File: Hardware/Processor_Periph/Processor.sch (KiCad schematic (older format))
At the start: 187 parts, among them J1 UART0, J10 JTAGICE3-SWD, J2 5V, J3 USB_OTG, J4 RJ-45_J0006D01BNL, J5 Micro_SD_Card, J6 I2C, J7 PWM, J8 Spare0, J9 Spare1, Q1 BSS806NE, Q2 BSS806NE, Q3 BSS806NE, Q4 BSS806NE, SW1 ~RST, SW2 PB, SW3 PB, U1 TXS0102, U10 Oscillator, U11 CY7C1018, U2 LM3671, U3 S25FL127S, U4 PRTR5V0U2X, U5 MIC5365, U6 DSC61XX, U7 DP83848C, U8 ATSAM4E16E, U9 3.0V, Y1 32.768kHz

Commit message: Fixed ERC issues, added reverse polarity protection diode
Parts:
- removed R32, R33: 0R, symbol R
- added D6: PMEG6030ETP, FritzLib:SOD-128, symbol D_Schottky_Small_ALT
- added R27, R34, R35: 0R, symbol R
- renumbered R34 to R24, R24 to R25, R25 to R26, R26 to R28, R27 to R29, R28 to R30, R29 to R31, R30 to R32, R31 to R33, R35 to R36, R36 to R37, R37 to R38, R38 to R39, R39 to R40, R40 to R41, R41 to R42, R42 to R43, R43 to R44, R44 to R45, R45 to R46, R46 to R47, R47 to R48, R48 to R49, R49 to R50, R50 to R51, R51 to R52, R52 to R53, R53 to R54, R54 to R55, R55 to R56, R56 to R57, R57 to R58, R58 to R59, R59 to R60, R60 to R61, R61 to R62, R62 to R63, R63 to R64, R64 to R65, R65 to R66, R66 to R67, R67 to R68, R68 to R69, R69 to R70, R70 to R71, R71 to R72, R72 to R73, R73 to R74, R74 to R75, R75 to R76, R76 to R77, R77 to R78, R78 to R79, R79 to R80
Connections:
- net labels removed: PB1
- wire segments 796 -> 1014
- no-connect marks 15 -> 16
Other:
- note added: "Replace 0R w/Ferrite \nBeads if EMI is an issue"
- moved on the sheet: J2, R24, R49, R50, R51, R52, R54, R55, R56, R57, R60, R61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

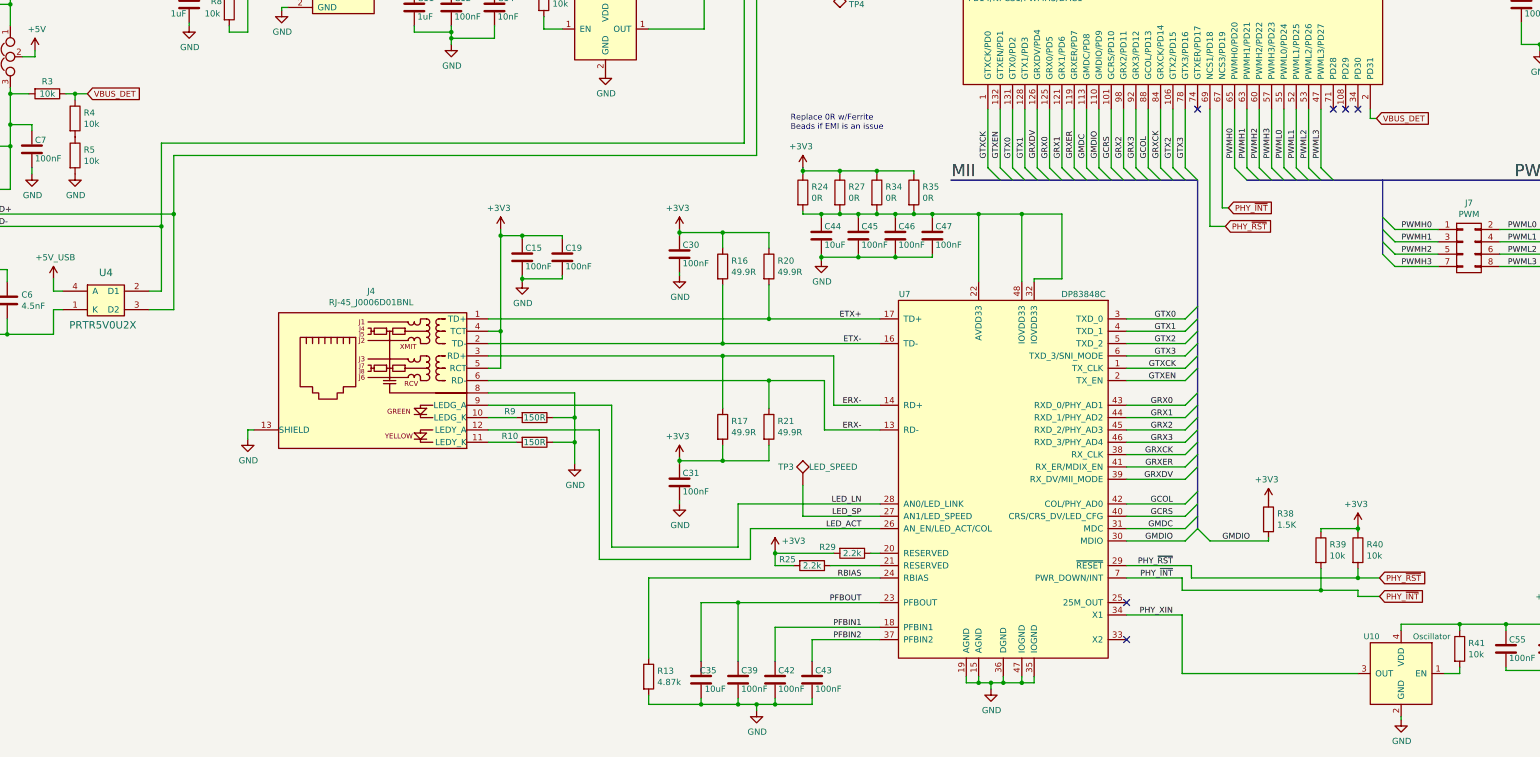
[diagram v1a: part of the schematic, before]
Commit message: Cleaned up schematic
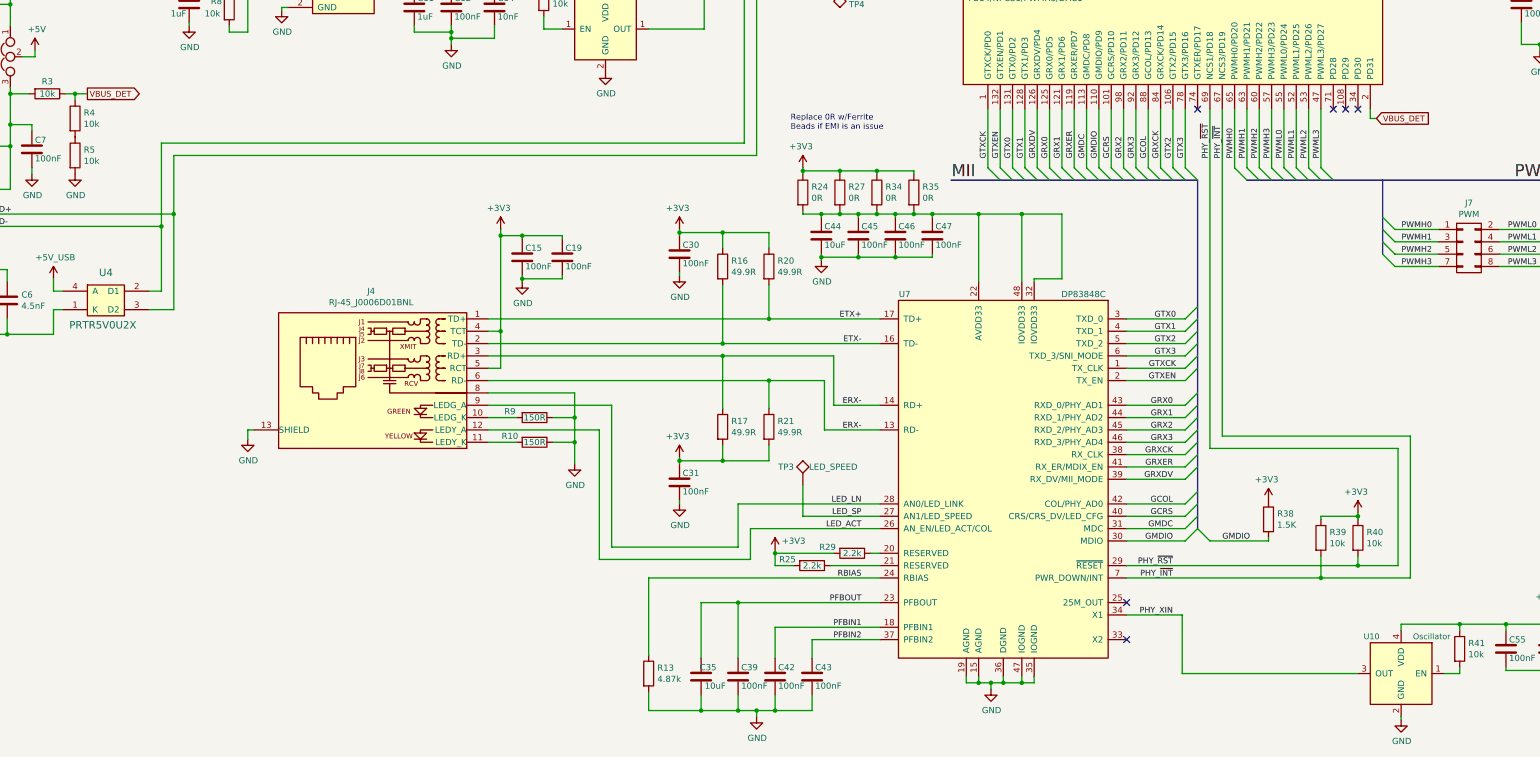
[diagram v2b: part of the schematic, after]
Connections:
- wire segments 1014 -> 1010
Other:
- moved on the sheet: C35, C39, C42, C43, R13, R39, R40
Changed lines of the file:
@@
 Text GLabel 14025 10150 2    47   Input ~ 0
 VBUS_DET
-Text GLabel 3575 9950 2    47   Input ~ 0
+Text GLabel 3575 9950 2    47   Output ~ 0
 VBUS_DET
 $Comp
@@
 L C C35
 U 1 1 58C1B446
-P 8550 14700
-F 0 "C35" H 8425 14775 50  0000 L CNN
-F 1 "10uF" H 8350 14625 50  0000 L CNN
-F 2 "Capacitors_SMD:C_0805" H -1737 9625 50  0001 C CNN
-F 3 "" H -1775 9775 50  0001 C CNN
-	1    8550 14700
+P 8550 14675
+F 0 "C35" H 8425 14750 50  0000 L CNN
+F 1 "10uF" H 8350 14600 50  0000 L CNN
+F 2 "Capacitors_SMD:C_0805" H -1737 9600 50  0001 C CNN
+F 3 "" H -1775 9750 50  0001 C CNN
+	1    8550 14675
 	-1   0    0    -1
 $EndComp
@@
 L C C39
 U 1 1 58C22208
-P 8850 14700
-F 0 "C39" H 8875 14775 50  0000 L CNN
-F 1 "100nF" H 8875 14625 50  0000 L CNN
-F 2 "Capacitors_SMD:C_0603" H -1437 9625 50  0001 C CNN
-F 3 "" H -1475 9775 50  0001 C CNN
-	1    8850 14700
+P 8850 14675
+F 0 "C39" H 8875 14750 50  0000 L CNN
+F 1 "100nF" H 8875 14600 50  0000 L CNN
+F 2 "Capacitors_SMD:C_0603" H -1437 9600 50  0001 C CNN
+F 3 "" H -1475 9750 50  0001 C CNN
+	1    8850 14675
 	1    0    0    -1
 $EndComp
@@
 L C C42
 U 1 1 58C243AA
-P 9150 14700
-F 0 "C42" H 9175 14775 50  0000 L CNN
-F 1 "100nF" H 9175 14625 50  0000 L CNN
-F 2 "Capacitors_SMD:C_0603" H -1137 9625 50  0001 C CNN
-F 3 "" H -1175 9775 50  0001 C CNN
-	1    9150 14700
+P 9150 14675
+F 0 "C42" H 9175 14750 50  0000 L CNN
+F 1 "100nF" H 9175 14600 50  0000 L CNN
+F 2 "Capacitors_SMD:C_0603" H -1137 9600 50  0001 C CNN
+F 3 "" H -1175 9750 50  0001 C CNN
+	1    9150 14675
 	1    0    0    -1
 $EndComp
@@
 L C C43
 U 1 1 58C24AF8
-P 9450 14700
-F 0 "C43" H 9475 14775 50  0000 L CNN
-F 1 "100nF" H 9475 14625 50  0000 L CNN
-F 2 "Capacitors_SMD:C_0603" H -837 9625 50  0001 C CNN
-F 3 "" H -875 9775 50  0001 C CNN
-	1    9450 14700
+P 9450 14675
+F 0 "C43" H 9475 14750 50  0000 L CNN
+F 1 "100nF" H 9475 14600 50  0000 L CNN
+F 2 "Capacitors_SMD:C_0603" H -837 9600 50  0001 C CNN
+F 3 "" H -875 9750 50  0001 C CNN
+	1    9450 14675
 	1    0    0    -1
 $EndComp
@@
 L GND #PWR064
 U 1 1 58C251B2
-P 9000 14950
-F 0 "#PWR064" H 6950 7900 50  0001 C CNN
-F 1 "GND" H 9005 14777 50  0000 C CNN
-F 2 "" H 6950 8150 50  0001 C CNN
-F 3 "" H 6950 8150 50  0001 C CNN
-	1    9000 14950
+P 9000 15000
+F 0 "#PWR064" H 6950 7950 50  0001 C CNN
+F 1 "GND" H 9005 14827 50  0000 C CNN
+F 2 "" H 6950 8200 50  0001 C CNN
+F 3 "" H 6950 8200 50  0001 C CNN
+	1    9000 15000
 	1    0    0    -1
 $EndComp
@@
 L R R40
 U 1 1 58FCC7EB
-P 13875 13650
-F 0 "R40" H 13945 13696 50  0000 L CNN
-F 1 "10k" H 13945 13605 50  0000 L CNN
-F 2 "Capacitors_SMD:C_0603" V 11805 5675 50  0001 C CNN
-F 3 "" H 11875 5675 50  0001 C CNN
-	1    13875 13650
+P 13875 13550
+F 0 "R40" H 13945 13596 50  0000 L CNN
+F 1 "10k" H 13945 13505 50  0000 L CNN
+F 2 "Capacitors_SMD:C_0603" V 11805 5575 50  0001 C CNN
+F 3 "" H 11875 5575 50  0001 C CNN
+	1    13875 13550
 	1    0    0    -1
 $EndComp
@@
 L +3V3 #PWR085
 U 1 1 58FCE5C3
-P 13875 13450
-F 0 "#PWR085" H 13925 13500 50  0001 C CNN
-F 1 "+3V3" H 13890 13623 50  0000 C CNN
-F 2 "" H 4150 9225 50  0001 C CNN
-F 3 "" H 4150 9225 50  0001 C CNN
-	1    13875 13450
+P 13875 13350
+F 0 "#PWR085" H 13925 13400 50  0001 C CNN
+F 1 "+3V3" H 13890 13523 50  0000 C CNN
+F 2 "" H 4150 9125 50  0001 C CNN
+F 3 "" H 4150 9125 50  0001 C CNN
+	1    13875 13350
 	-1   0    0    -1
 $EndComp
 Text Label 12375 13775 2    47   ~ 0
 PHY_~RST
-Text GLabel 14050 13875 2    47   Input ~ 0
-PHY_~RST
-Text GLabel 12800 11025 2    47   Input ~ 0
-PHY_~RST
 $Comp
 L R R22
@@
 Text Label 10075 4775 0    47   ~ 0
 I2C_SDA
-Text GLabel 14050 14025 2    47   Input ~ 0
-PHY_~INT
 Entry Wire Line
 	12675 13575 12575 13475
@@
 L R R39
 U 1 1 59087037
-P 13575 13650
-F 0 "R39" H 13645 13696 50  0000 L CNN
-F 1 "10k" H 13645 13605 50  0000 L CNN
-F 2 "Capacitors_SMD:C_0603" V 11505 5675 50  0001 C CNN
-F 3 "" H 11575 5675 50  0001 C CNN
-	1    13575 13650
+P 13575 13550
+F 0 "R39" H 13645 13596 50  0000 L CNN
+F 1 "10k" H 13645 13505 50  0000 L CNN
+F 2 "Capacitors_SMD:C_0603" V 11505 5575 50  0001 C CNN
+F 3 "" H 11575 5575 50  0001 C CNN
+	1    13575 13550
 	1    0    0    -1
 $EndComp
@@
 L R R13
 U 1 1 5908C698
-P 8125 14675
-F 0 "R13" H 8195 14721 50  0000 L CNN
-F 1 "4.87k" H 8195 14630 50  0000 L CNN
-F 2 "" V 8055 14675 50  0001 C CNN
-F 3 "" H 8125 14675 50  0001 C CNN
-	1    8125 14675
+P 8125 14650
+F 0 "R13" H 8195 14696 50  0000 L CNN
+F 1 "4.87k" H 8195 14605 50  0000 L CNN
+F 2 "" V 8055 14650 50  0001 C CNN
+F 3 "" H 8125 14650 50  0001 C CNN
+	1    8125 14650
 	1    0    0    -1
 $EndComp
@@
 Text Label 21900 13925 2    47   ~ 0
 GRXER
-Text GLabel 12825 10875 2    47   Input ~ 0
-PHY_~INT
 NoConn ~ 12575 10075
 NoConn ~ 10475 8575
@@
 	13675 10650 15475 10650
 Wire Wire Line
-	12775 10875 12825 10875
-Wire Wire Line
-	12775 10075 12775 10875
+	12775 10075 12775 12725
 Wire Notes Line
 	22100 12675 22100 12925
@@
 	8125 13875 10000 13875
 Wire Wire Line
-	8125 14525 8125 13875
-Connection ~ 8550 14900
+	8125 14500 8125 13875
+Connection ~ 8550 14950
 Wire Wire Line
-	8125 14825 8125 14900
-Connection ~ 13875 13475
+	8125 14800 8125 14950
+Connection ~ 13875 13375
 Wire Wire Line
-	13575 13475 13575 13500
+	13575 13375 13575 13400
 Wire Wire Line
-	13875 13475 13575 13475
-Connection ~ 13575 13975
+	13875 13375 13575 13375
+Connection ~ 13575 13875
 Wire Wire Line
-	13575 13800 13575 13975
+	13575 13700 13575 13875
 Wire Wire Line
 	9375 13375 10000 13375
@@
 	13150 13575 13150 13550
 Wire Wire Line
-	12450 13975 13575 13975
-Wire Wire Line
-	13575 13975 13875 13975
-Wire Wire Line
-	12450 13875 12450 13975
-Wire Wire Line
-	12000 13875 12450 13875
-Wire Wire Line
-	12525 13875 13875 13875
+	12000 13875 13575 13875
 Wire Wire Line
-	13875 13875 14050 13875
+	13575 13875 14300 13875
 Wire Wire Line
-	12525 13775 12525 13875
+	12000 13775 13875 13775
 Wire Wire Line
-	12000 13775 12525 13775
+	13875 13775 14200 13775
 Wire Wire Line
 	12675 13575 13150 13575
-Wire Wire Line
-	13875 14025 14050 14025
-Wire Wire Line
-	13875 13975 13875 14025
 Connection ~ 9075 4575
 Connection ~ 9675 4675
@@
 	9025 4175 9025 4150
 Wire Wire Line
-	12675 11025 12800 11025
-Wire Wire Line
-	12675 10075 12675 11025
-Connection ~ 13875 13875
+	12675 10075 12675 12825
+Connection ~ 13875 13775
 Wire Wire Line
-	13875 13450 13875 13475
+	13875 13350 13875 13375
 Wire Wire Line
-	13875 13475 13875 13500
+	13875 13375 13875 13400
 Wire Wire Line
-	13875 13875 13875 13800
+	13875 13775 13875 13700
 Connection ~ 7525 12575
 Wire Wire Line
@@
 Connection ~ 8850 14075
 Wire Wire Line
-	8550 14550 8550 14075
+	8550 14525 8550 14075
 Wire Wire Line
 	8550 14075 8850 14075
@@
 	8850 14075 10000 14075
 Wire Wire Line
-	8850 14550 8850 14075
+	8850 14525 8850 14075
 Wire Wire Line
-	9150 14275 9150 14550
+	9150 14275 9150 14525
 Wire Wire Line
 	10000 14275 9150 14275
 Wire Wire Line
-	9450 14375 9450 14550
+	9450 14375 9450 14525
 Wire Wire Line
 	10000 14375 9450 14375
-Connection ~ 9000 14900
-Connection ~ 8850 14900
+Connection ~ 9000 14950
+Connection ~ 8850 14950
 Wire Wire Line
-	8850 14900 8850 14850
-Connection ~ 9150 14900
+	8850 14950 8850 14825
+Connection ~ 9150 14950
 Wire Wire Line
-	9450 14900 9450 14850
+	9450 14950 9450 14825
 Wire Wire Line
-	9150 14900 9150 14850
+	9150 14950 9150 14825
 Wire Wire Line
-	9000 14900 9000 14950
+	9000 14950 9000 15000
 Wire Wire Line
-	8125 14900 8550 14900
+	8125 14950 8550 14950
 Wire Wire Line
-	8550 14900 8850 14900
+	8550 14950 8850 14950
 Wire Wire Line
-	8850 14900 9000 14900
+	8850 14950 9000 14950
 Wire Wire Line
-	9000 14900 9150 14900
+	9000 14950 9150 14950
 Wire Wire Line
-	9150 14900 9450 14900
+	9150 14950 9450 14950
 Wire Wire Line
-	8550 14850 8550 14900
+	8550 14825 8550 14950
 Connection ~ 2175 6850
 Wire Wire Line
@@
 	11250 11450 11475 11450
 Wire Wire Line
-	11475 11450 11475 10925
+	11475 10925 11475 11450
 Connection ~ 10800 10925
 Connection ~ 11150 10925
@@
 $EndComp
 Wire Wire Line
-	11475 10925 11150 10925
+	9375 10925 9525 10925
 Wire Wire Line
-	11150 10925 10800 10925
+	9525 10925 9675 10925
 Wire Wire Line
-	10800 10925 10425 10925
+	9675 10925 9825 10925
 Wire Wire Line
-	10425 10925 10275 10925
+	9825 10925 9975 10925
 Wire Wire Line
-	10275 10925 10125 10925
+	9975 10925 10125 10925
 Wire Wire Line
-	10125 10925 9975 10925
+	10125 10925 10275 10925
 Wire Wire Line
-	9975 10925 9825 10925
+	10275 10925 10425 10925
 Wire Wire Line
-	9825 10925 9675 10925
+	10425 10925 10800 10925
 Wire Wire Line
-	9675 10925 9525 10925
+	10800 10925 11150 10925
 Wire Wire Line
-	9525 10925 9375 10925
+	11150 10925 11475 10925
 $Comp
 L R R27
@@
 Text Label 9575 6175 2    98   ~ 0
 EBI
+Text Label 12675 10475 1    47   ~ 0
+PHY_~RST
+Text Label 12775 10475 1    47   ~ 0
+PHY_~INT
+Wire Wire Line
+	14300 13875 14300 12725
+Wire Wire Line
+	14200 13775 14200 12825
+Wire Wire Line
+	14200 12825 12675 12825
+Wire Wire Line
+	14300 12725 12775 12725
 $EndSCHEMATC

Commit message: Added termination resistors to PHY & cleaned up schematic
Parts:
- added R? (x11): 33R, Capacitors_SMD:C_0603, symbol R
- U10: value Oscillator -> ASE-25.000MHZ-LC-T
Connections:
- net labels added: GCOL_R, GCRS_R, GMDC_R, GMDIO_R, GRX0_R, GRX1_R, GRX2_R, GRX3_R, GRXCK_R, GRXDV_R, GRXER_R
- wire segments 1010 -> 1021
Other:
- moved on the sheet: C10, C11, C12, C14, C15, C19, C2, C30, C31, C35, C39, C42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

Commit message: Updated BOM
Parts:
- removed J7: PWM, symbol CONN_02X04
- added J7: PWM, symbol CONN_02X06
- added R92: 0R, symbol R
- added TP11: XOUT_32, Measurement_Points:Measurement_Point_Round-SMD-Pad_Small, symbol TEST
- added TP12: XIN_32, Measurement_Points:Measurement_Point_Round-SMD-Pad_Small, symbol TEST
- added TP13: MCU_XIN, Measurement_Points:Measurement_Point_Round-SMD-Pad_Small, symbol TEST
- added TP14: PHY_XIN, Measurement_Points:Measurement_Point_Round-SMD-Pad_Small, symbol TEST
- R81, R82, R83, R84, R85, R86, R87, R88, R89, R90, R91: renamed from R?; value 33R -> 27R
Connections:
- wire segments 1021 -> 817

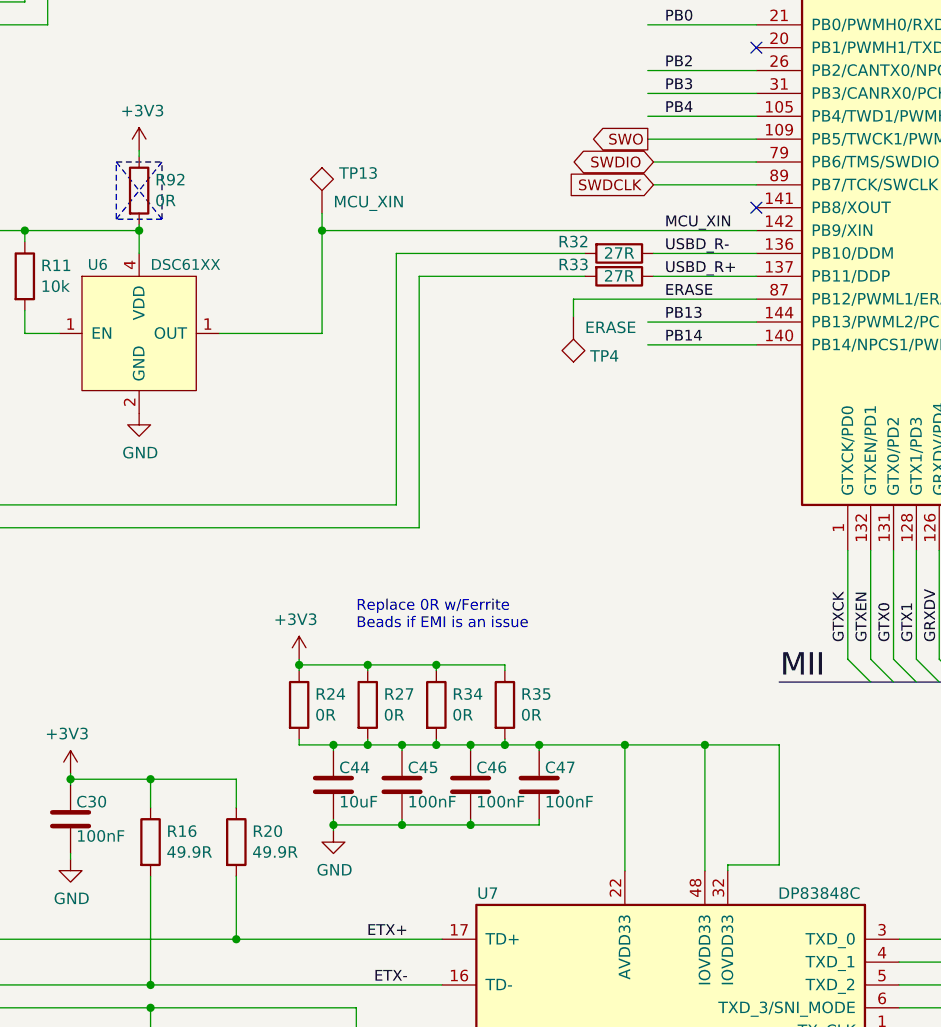
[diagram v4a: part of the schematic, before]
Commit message: Assigned some footprints, finished BOM
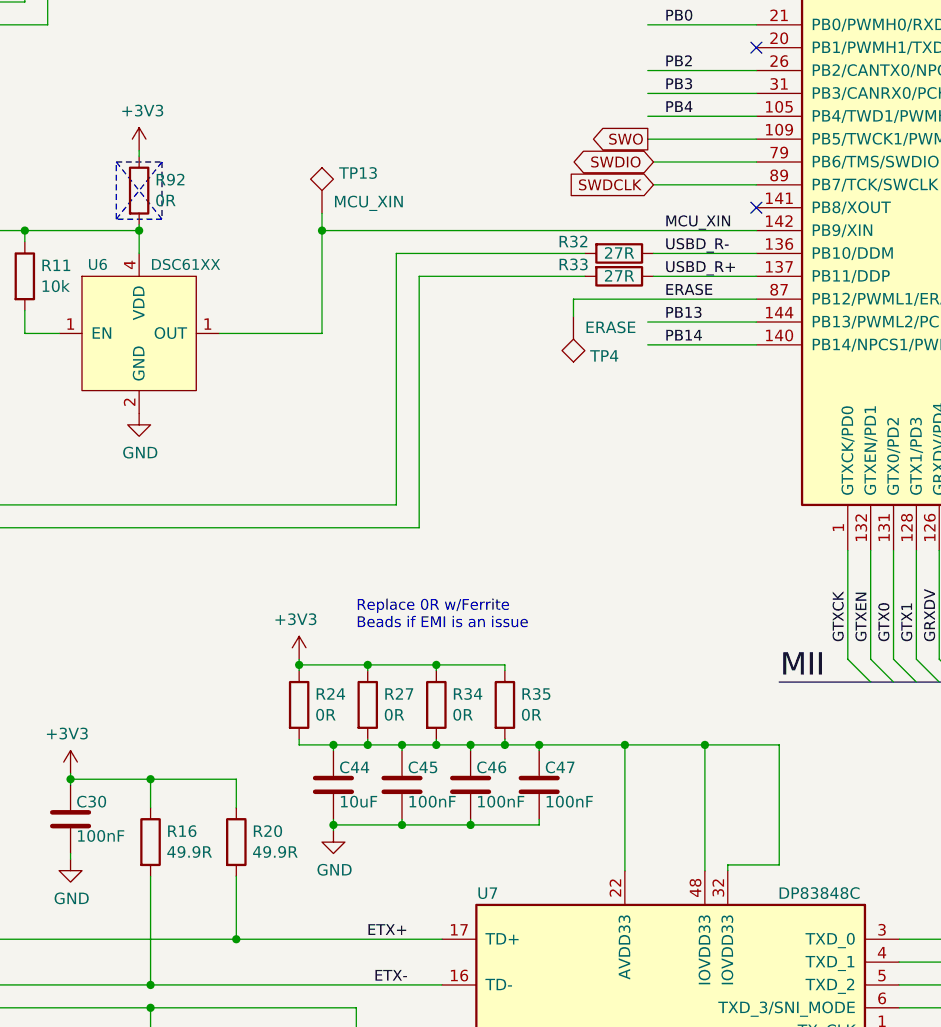
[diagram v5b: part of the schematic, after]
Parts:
- C10, C11, C44: footprint Capacitors_SMD:C_0603 -> Capacitors_SMD:C_0805
- D1, D2, D3, D4, D5: footprint LEDs:LED_0805 -> Diodes_SMD:D_0805
- J1: footprint FritzLib:ConnectorSMD-1x4 -> (none)
- J10: footprint FritzLib:ConnectorMicromatch-10 -> Pin_Headers:Pin_Header_Straight_2x05_Pitch1.27mm_SMD
- J2, JP1: footprint FritzLib:ConnectorSMD-1x3 -> (none)
- J3: footprint FritzLib:conn_usb_B_micro_smd -> (none)
- L1: footprint Inductors:Inductor_1212 -> (none)
- L2: footprint FritzLib:Inductor_3mmx3mm -> (none)
- Q1, Q2, Q3, Q4: footprint TO_SOT_Packages_SMD:SOT-23 -> (none)
- R1, R11, R12, R14, R15, R18, R19, R2, R22, R23, R25, R26, R28, R29, R3, R30, R31, R32, R33, R36, R37, R38, R39, R4, R40, R41, R42, R43, R44, R45, R46, R47, R48, R49, R5, R50, R51, R52, R54, R55, R56, R57, R58, R6, R60, R61, R62, R63, R64, R65, R66, R67, R68, R70, R71, R72, R73, R74, R75, R77, R78, R79, R8, R80, R81, R82, R83, R84, R85, R86, R87, R88, R89, R90, R91: footprint Capacitors_SMD:C_0603 -> Resistors_SMD:R_0603
- R10, R9: footprint Capacitors_SMD:C_0603 -> Resistors_SMD:R_0805
- R13, R16, R17, R20, R21, R24, R27, R34, R35, R92: footprint (none) -> Resistors_SMD:R_0603
- R53, R59, R69, R7, R76: footprint Capacitors_SMD:C_0805 -> Resistors_SMD:R_0805
- TP1, TP10, TP11, TP12, TP13, TP14, TP2, TP3, TP4, TP5, TP6, TP7, TP8, TP9: footprint Measurement_Points:Measurement_Point_Round-SMD-Pad_Small -> Measurement_Points:Test_Point_Keystone_5019_Minature
- U3: footprint (none) -> Housings_SOIC:SOIC-8_3.9x4.9mm_Pitch1.27mm
- U4: footprint FritzLib:SOT143B -> TO_SOT_Packages_SMD:SOT-143
- U5: footprint (none) -> TO_SOT_Packages_SMD:SOT-23-5
- U7: footprint LQFP-48 -> Housings_QFP:LQFP-48_7x7mm_Pitch0.5mm
- U8: footprint (none) -> Housings_QFP:TQFP-144_20x20mm_Pitch0.5mm
- Y1: footprint FritzLib:FC-135R -> (none)
